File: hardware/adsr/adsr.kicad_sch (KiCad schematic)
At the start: 63 parts, among them J1 MonoJack, J2 MonoJack, J4 Conn_02x05_Odd_Even, Q1 BC847, Q2 BC847, Q3 BC847, Q4 BC847, Q5 BC847, Q6 2N7002K, SW1 SW_DPDT_x2, SW2 SW_Push, U1 ICM7556, U2 TL074

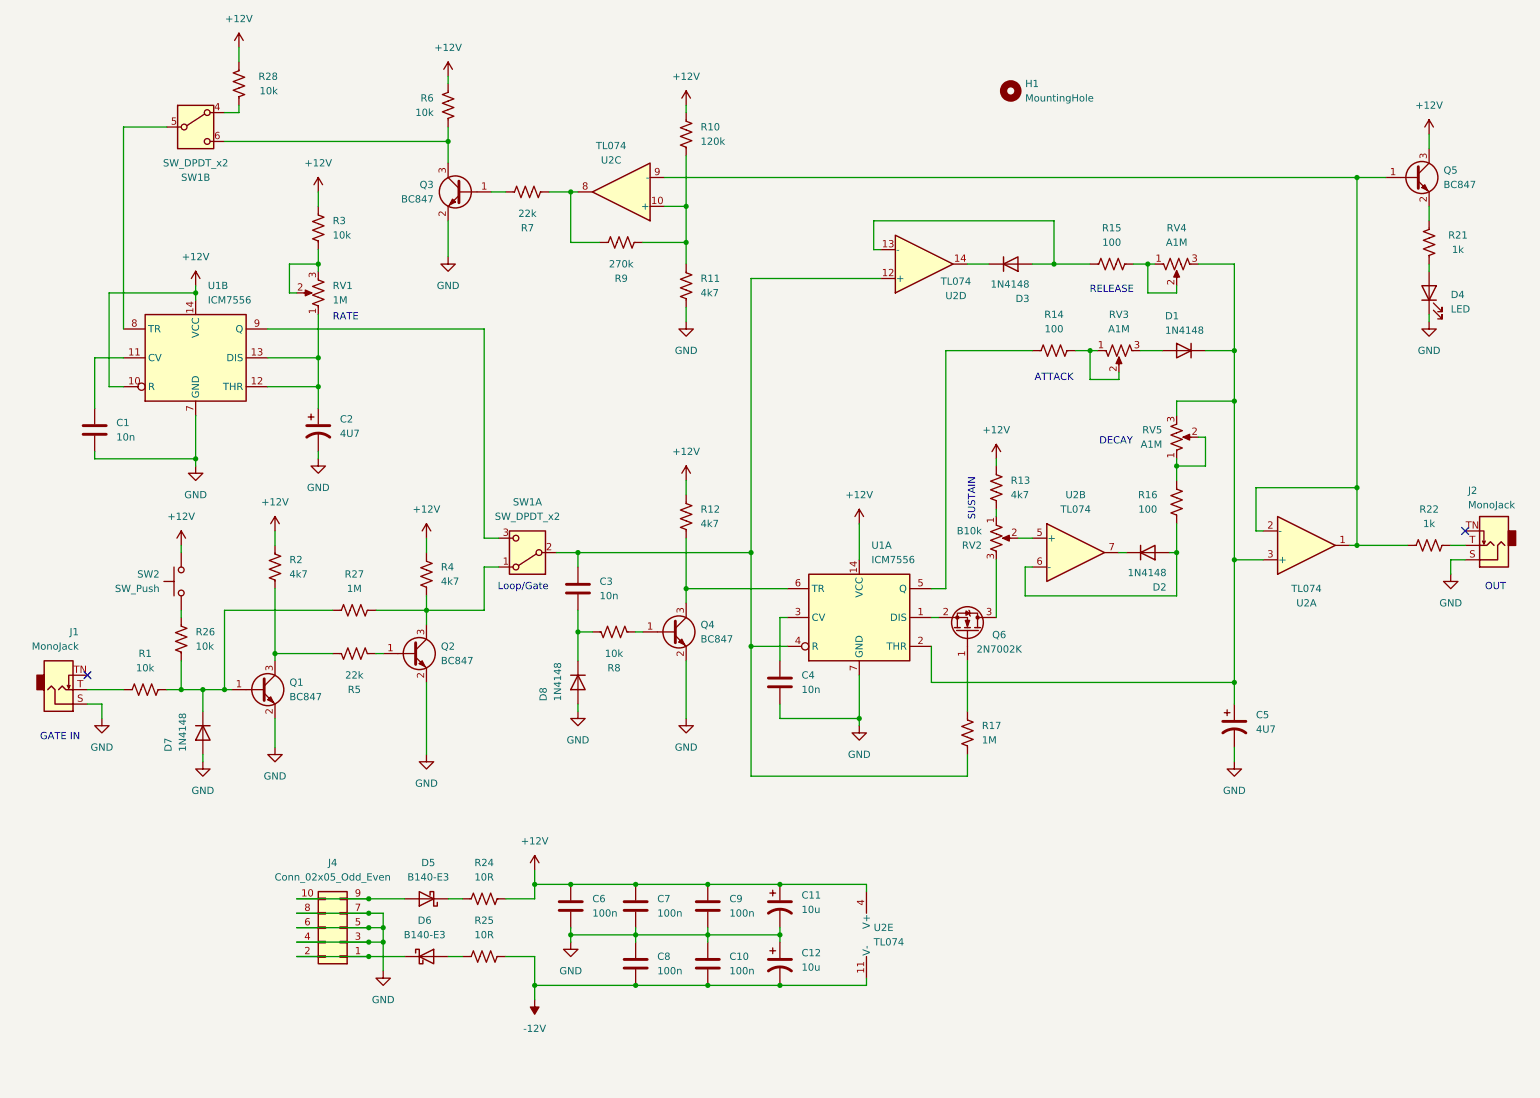
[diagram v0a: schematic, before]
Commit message: Feat/external trigger (#3)
* Committing WIP on ADSR with trigger: Falstad circuit & schematic, some changes to the KiCAD schematic 
* schematic built and tested on breadboard
* added schematic screenshot from Falstad and updated the simulation circuit (link)
* routed PCB, needs cleanup
* routing cleanup
* clean up silk, check board, generate gerbers for v2
* Updated documentation for trigger input
* Updated BOM
* Updated assembly guide after assembling and testing two boards. Added annotations to schematic.
* Faceplate with art. Tested with 3DP and printouts. Adjustments marked on layout.
* Clean up and regenerate schematic.pdf (out of date before)
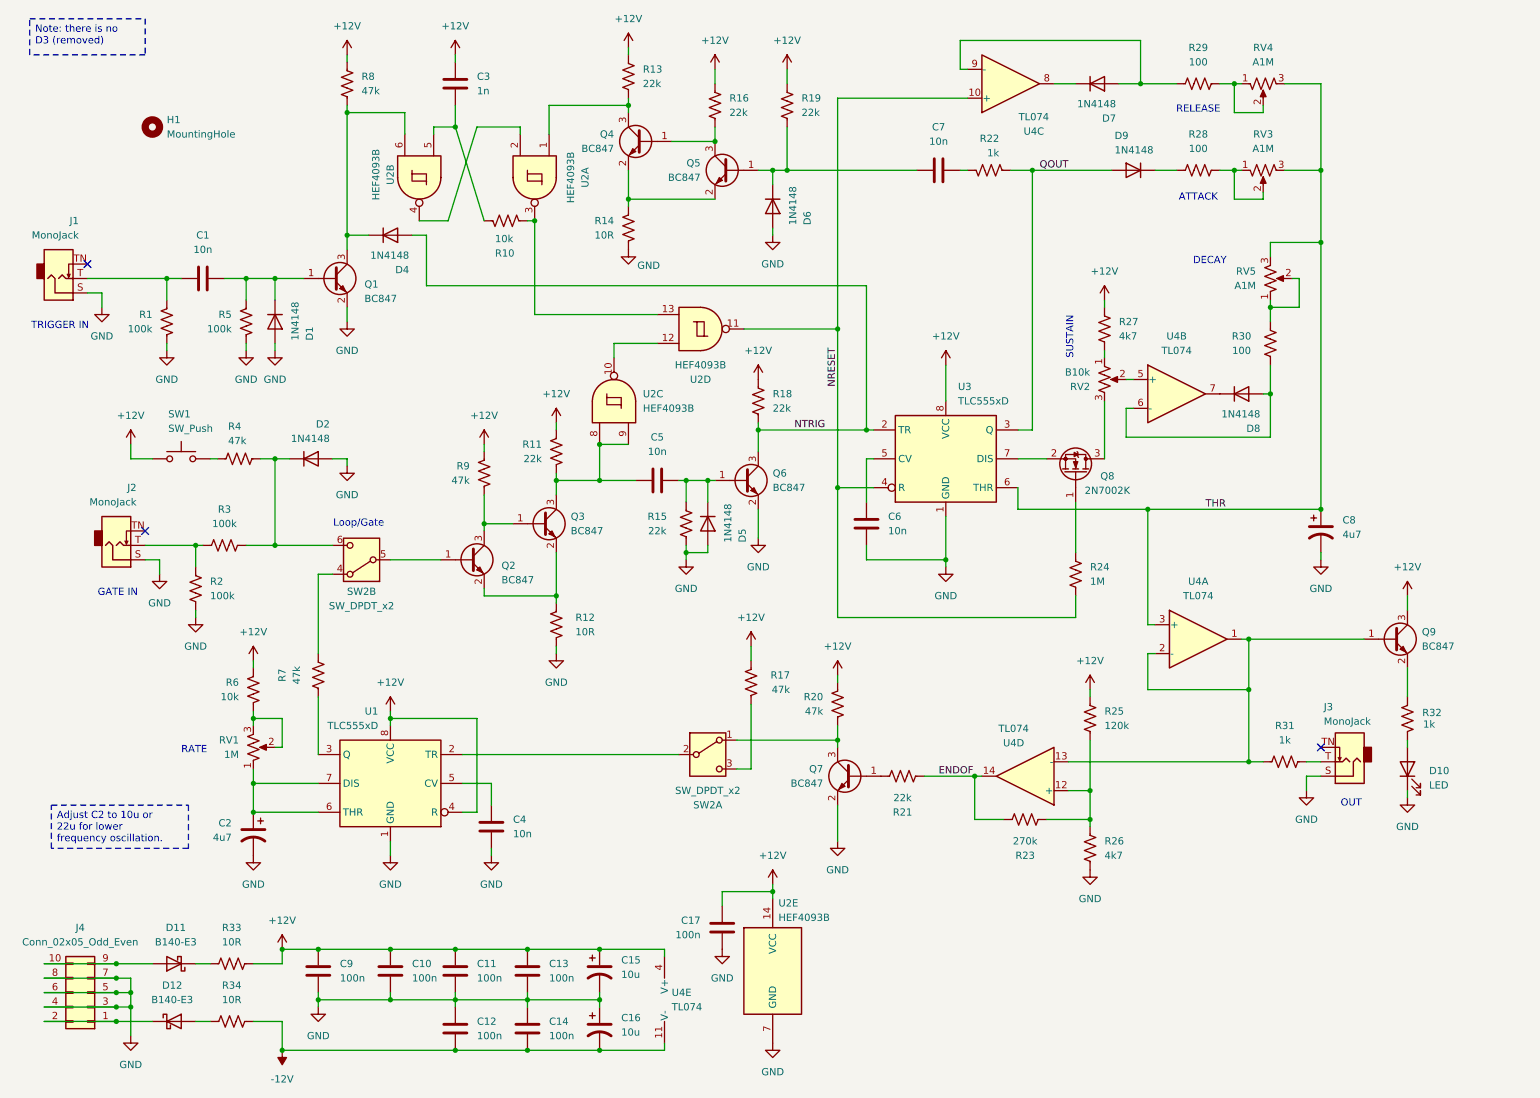
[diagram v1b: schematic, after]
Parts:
- removed D8: 1N4148, Diode_SMD:D_SOD-123, symbol Diode:1N4148
- removed R27: 1M, Resistor_SMD:R_0805_2012Metric_Pad1.20x1.40mm_HandSolder, symbol Device:R_US
- removed SW1: SW_DPDT_x2, Switches:SW_Dailywell_DPDT_2MD1T1B1M1, symbol Switch:SW_DPDT_x2
- removed U1: ICM7556, Package_SO:SOIC-14_3.9x8.7mm_P1.27mm, symbol Timer:ICM7556
- removed unit 1 of U2
- removed unit 3 of U2
- added C1, C7: 10n, Capacitor_SMD:C_0805_2012Metric_Pad1.18x1.45mm_HandSolder, symbol Device:C
- added C10, C17: 100n, Capacitor_SMD:C_0805_2012Metric_Pad1.18x1.45mm_HandSolder, symbol Device:C
- added C3: 1n, Capacitor_SMD:C_0805_2012Metric_Pad1.18x1.45mm_HandSolder, symbol Device:C
- added D1, D4, D5, D6: 1N4148, Diode_SMD:D_SOD-123, symbol Diode:1N4148
- added J1: MonoJack, AudioJacks:Jack_3.5mm_QingPu_WQP-PJ301M-12_Vertical, symbol Connector_Audio:AudioJack2_SwitchT
- added Q1, Q4, Q5: BC847, Package_TO_SOT_SMD:SOT-23, symbol Transistor_BJT:BC847
- added R1, R2, R5: 100k, Resistor_SMD:R_0805_2012Metric_Pad1.20x1.40mm_HandSolder, symbol Device:R_US
- added R10: 10k, Resistor_SMD:R_0805_2012Metric_Pad1.20x1.40mm_HandSolder, symbol Device:R_US
- added R13, R16, R19: 22k, Resistor_SMD:R_0805_2012Metric_Pad1.20x1.40mm_HandSolder, symbol Device:R_US
- added R14: 10R, Resistor_SMD:R_0805_2012Metric_Pad1.20x1.40mm_HandSolder, symbol Device:R_US
- added R22: 1k, Resistor_SMD:R_0805_2012Metric_Pad1.20x1.40mm_HandSolder, symbol Device:R_US
- added R7, R8: 47k, Resistor_SMD:R_0805_2012Metric_Pad1.20x1.40mm_HandSolder, symbol Device:R_US
- added SW2: SW_DPDT_x2, Switches:SW_Dailywell_DPDT_2MD1T1B1M1, symbol Switch:SW_DPDT_x2
- added U1, U3: TLC555xD, Package_SO:SOIC-8_3.9x4.9mm_P1.27mm, symbol Timer:TLC555xD
- added U2: HEF4093B, Package_SO:SOIC-14_3.9x8.7mm_P1.27mm, symbol 4xxx:HEF4093B
- added unit 1 of U4
- added unit 3 of U4
- C2: value 4U7 -> 4u7
- C8: renamed from C5; value 4U7 -> 4u7
- R11: renamed from R4; value 4k7 -> 22k
- R12: renamed from R5; value 22k -> 10R
- R15: renamed from R8; value 10k -> 22k
- R17: renamed from R28; value 10k -> 47k
- R18: renamed from R12; value 4k7 -> 22k
- R20: renamed from R6; value 10k -> 47k
- R3: renamed from R1; value 10k -> 100k
- R4: renamed from R26; value 10k -> 47k
- R9: renamed from R2; value 4k7 -> 47k
- RV1, RV2, RV3, RV4, RV5: footprint Potentiometer_THT:Potentiometer_Bourns_PTV09A-1_Single_Vertical -> Audio_Potentiometer_THT:Potentiometer_Bourns_PTV09A-1_Single_Vertical_thin
- renumbered C7 to C11, C8 to C12, C9 to C13, C10 to C14, C11 to C15, C12 to C16, C1 to C4, C3 to C5, C4 to C6, C6 to C9, D4 to D10, D5 to D11, D6 to D12, D7 to D2, D3 to D7, D2 to D8, D1 to D9, J1 to J2, J2 to J3, Q1 to Q2, Q2 to Q3, Q4 to Q6, Q3 to Q7, Q6 to Q8, Q5 to Q9, R7 to R21, R9 to R23, R17 to R24, R10 to R25, R11 to R26, R13 to R27, R14 to R28, R15 to R29, R16 to R30, R22 to R31, R21 to R32, R24 to R33, R25 to R34, R3 to R6, SW2 to SW1, U2 to U4
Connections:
- net +12V: now also SW1.2, C10.2, C17.2, C3.2, R13.1, R16.1, R19.1, R8.2, U1.4 (R), U1.8 (VCC), U2.14 (VCC), U3.8 (VCC); no longer SW1.1
- net GND: now also R12.2, R15.2, C10.1, C17.1, D1.2 (A), D5.2 (A), D6.2 (A), J1.S, Q1.2 (E), R1.1, R14.1, R2.1, R5.1, U1.1 (GND), U2.7 (GND), U3.1 (GND); no longer Q2.2 (E), Q3.2 (E)
- net at Q9.1 (B), R31.1: now also U4.13 (-), U4.1, U4.2 (-)
- net THR: now reaches C8.1, RV4.3, RV5.3
- net THR: now also RV3.3, U3.6 (THR), U4.3 (+); no longer D9.1 (K)
- net at J2.T, R3.1: now also R2.2
- net at D2.1 (K), R3.2, R4.1: now also SW2.6 (C); no longer Q2.1 (B)
- net at R23.1, R25.1, R26.2: now also U4.12 (+)
- net at C4.2: now also U1.5 (CV)
- net at Q8.2 (S): now also U3.7 (DIS)
- net at Q3.1 (B): now also Q2.3 (C), R9.1; no longer R12.1
- net at Q3.3 (C), R11.2: now also C5.2, U2.8, U2.9
- net at C2.1, RV1.1: now also U1.6 (THR), U1.7 (DIS)
- net at Q6.1 (B), R15.1: now also C5.1, D5.1 (K)
- net NTRIG: now reaches Q6.3 (C), R18.2
- net NTRIG: now also D4.2 (A), U3.2 (TR)
- net ENDOF: now reaches R21.2, R23.2
- net ENDOF: now also U4.14
- net at D7.2 (A), R29.1: now also U4.9 (-); no longer U4.13 (-)
- net at D7.1 (K): now also U4.8; no longer U4.14
- net at R28.1: now also D9.1 (K)
- net at Q7.3 (C), R20.2: now also SW2.1 (A)
- net at R17.2: now also SW2.3 (C)
- net at R4.2: now also SW1.1; no longer SW1.2
- net at C6.2: now also U3.5 (CV)
- net QOUT: now reaches D9.2 (A)
- net QOUT: now also R22.2, U3.3 (Q); no longer RV3.3
- new net: C1.1, D1.1 (K), Q1.1 (B), R5.2
- new net: SW2.2 (B), U1.2 (TR)
- new net: R7.2, U1.3 (Q)
- new net: C7.1, R22.1
- new net: Q2.2 (E), Q3.2 (E), R12.1
- new net: C3.1, R10.2, U2.5
- new net: Q4.3 (C), R13.2, U2.1
- new net: U2.2, U2.4
- new net: R10.1, U2.13, U2.3
- new net: C7.2, D6.1 (K), Q5.1 (B), R19.2
- new net: Q4.2 (E), Q5.2 (E), R14.2
- new net: Q4.1 (B), Q5.3 (C), R16.2
- new net: R7.1, SW2.4 (A)
- new net: Q2.1 (B), SW2.5 (B)
- new net: U2.10, U2.12
- new net: C1.2, J1.T, R1.2
- new net: D4.1 (K), Q1.3 (C), R8.1, U2.6
- new net NRESET: R24.2, U2.11, U3.4 (R), U4.10 (+)
- no-connect marks 2 -> 3
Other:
- note added: "TRIGGER IN"
- moved on the sheet: C11, C12, C13, C14, C15, C16, C2, C4, C5, C6, C8, C9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

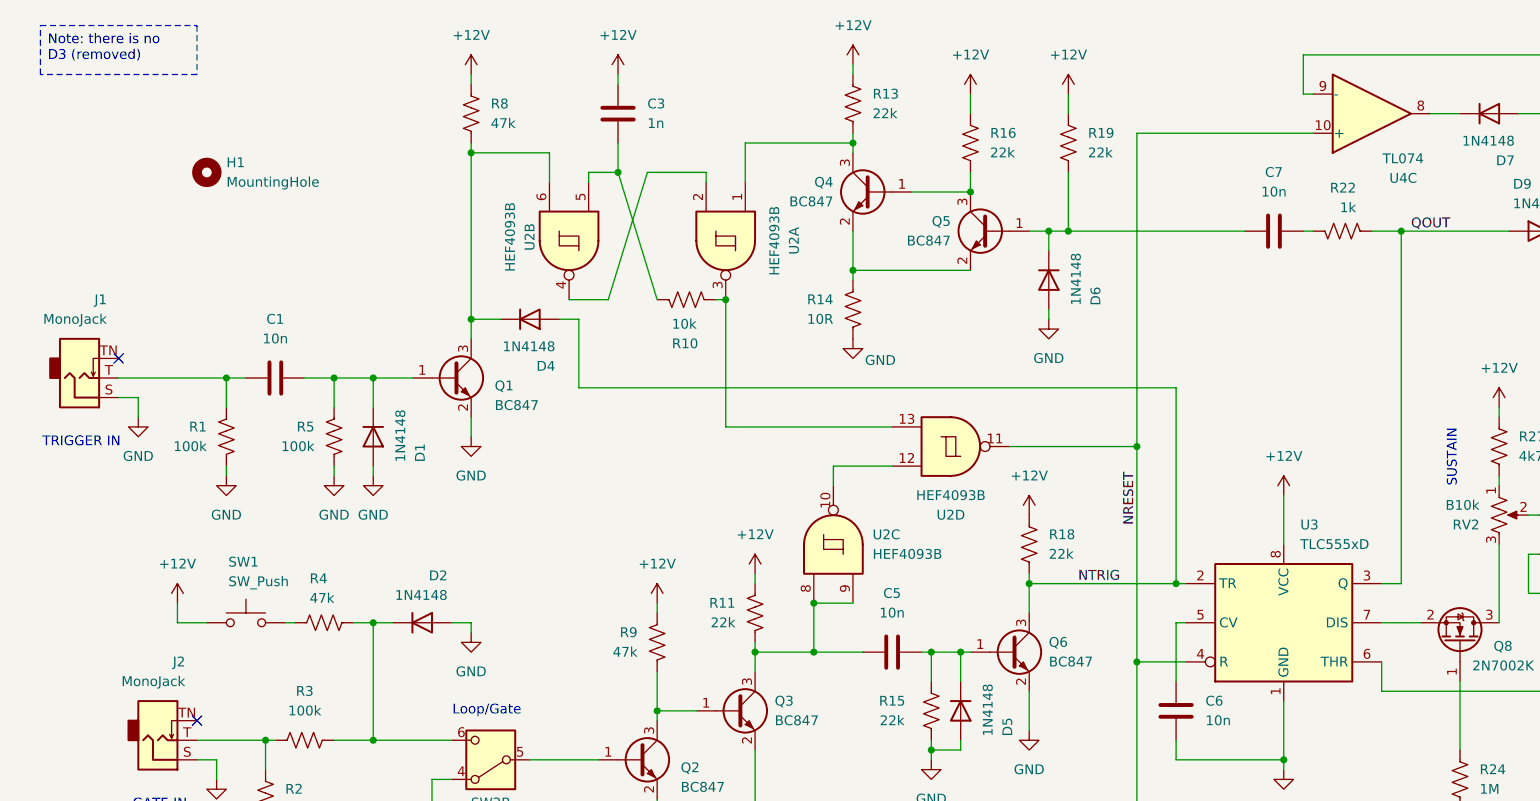
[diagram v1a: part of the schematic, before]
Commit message: Redrawing the schematic to show how the trigger could be added as an extension. Not implemented/tested.
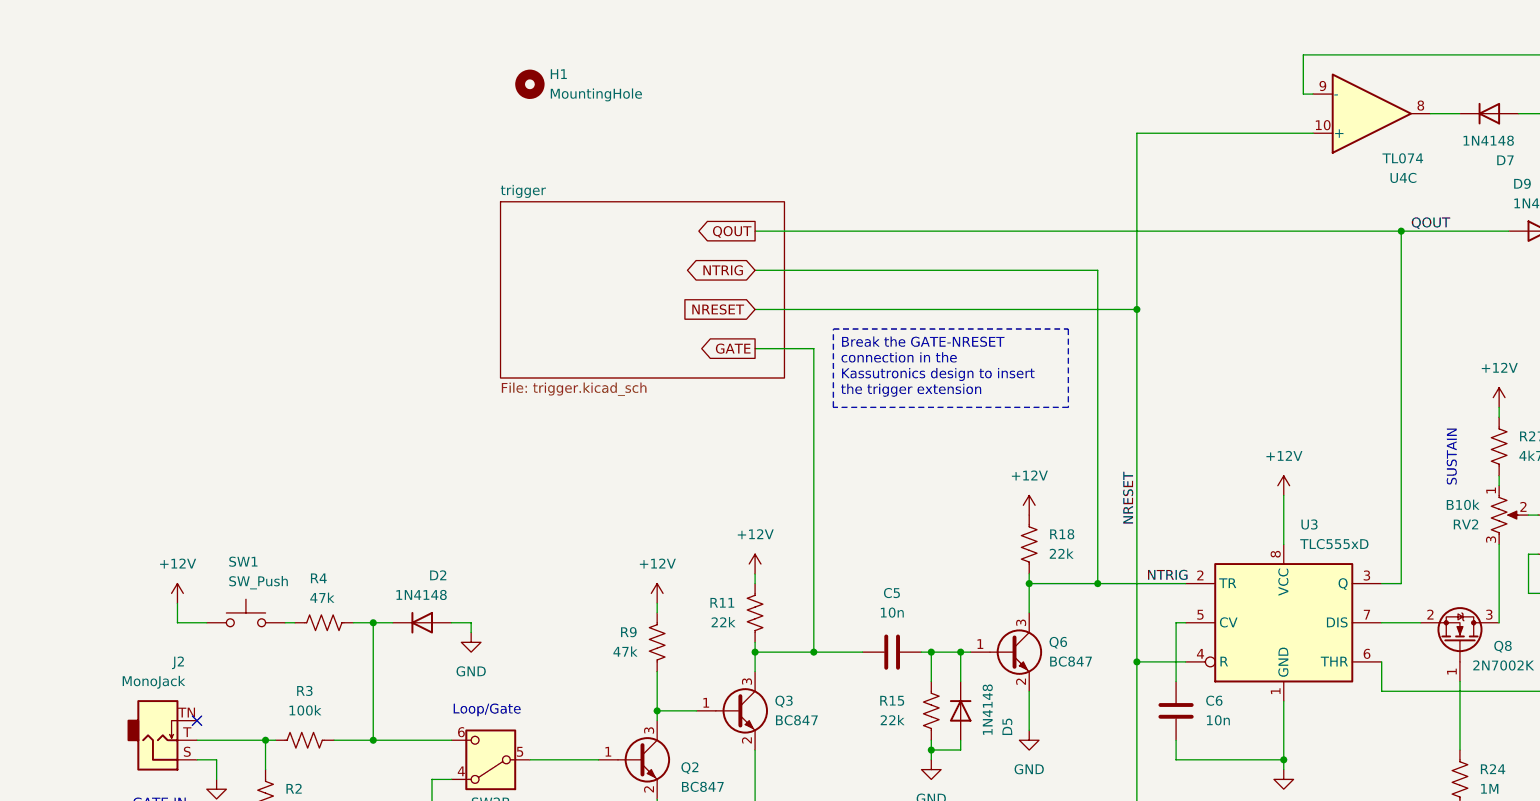
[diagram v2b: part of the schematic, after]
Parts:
- removed C1, C7: 10n, Capacitor_SMD:C_0805_2012Metric_Pad1.18x1.45mm_HandSolder, symbol Device:C
- removed C3: 1n, Capacitor_SMD:C_0805_2012Metric_Pad1.18x1.45mm_HandSolder, symbol Device:C
- removed D1, D4, D6: 1N4148, Diode_SMD:D_SOD-123, symbol Diode:1N4148
- removed J1: MonoJack, AudioJacks:Jack_3.5mm_QingPu_WQP-PJ301M-12_Vertical, symbol Connector_Audio:AudioJack2_SwitchT
- removed Q1, Q4, Q5: BC847, Package_TO_SOT_SMD:SOT-23, symbol Transistor_BJT:BC847
- removed R1, R5: 100k, Resistor_SMD:R_0805_2012Metric_Pad1.20x1.40mm_HandSolder, symbol Device:R_US
- removed R10: 10k, Resistor_SMD:R_0805_2012Metric_Pad1.20x1.40mm_HandSolder, symbol Device:R_US
- removed R13, R16, R19: 22k, Resistor_SMD:R_0805_2012Metric_Pad1.20x1.40mm_HandSolder, symbol Device:R_US
- removed R14: 10R, Resistor_SMD:R_0805_2012Metric_Pad1.20x1.40mm_HandSolder, symbol Device:R_US
- removed R22: 1k, Resistor_SMD:R_0805_2012Metric_Pad1.20x1.40mm_HandSolder, symbol Device:R_US
- removed R8: 47k, Resistor_SMD:R_0805_2012Metric_Pad1.20x1.40mm_HandSolder, symbol Device:R_US
- removed unit 1 of U2
- removed unit 4 of U2
- removed unit 3 of U2
- removed unit 2 of U2
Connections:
- net GATE: now reaches C5.2, Q3.3 (C), R11.2
- no-connect marks 3 -> 2
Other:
- added sheet trigger (trigger.kicad_sch)
- note removed: "TRIGGER IN"
- moved on the sheet: H1
